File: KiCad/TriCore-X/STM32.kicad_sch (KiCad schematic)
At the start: 1 part, among them U7 STM32H723VGHx

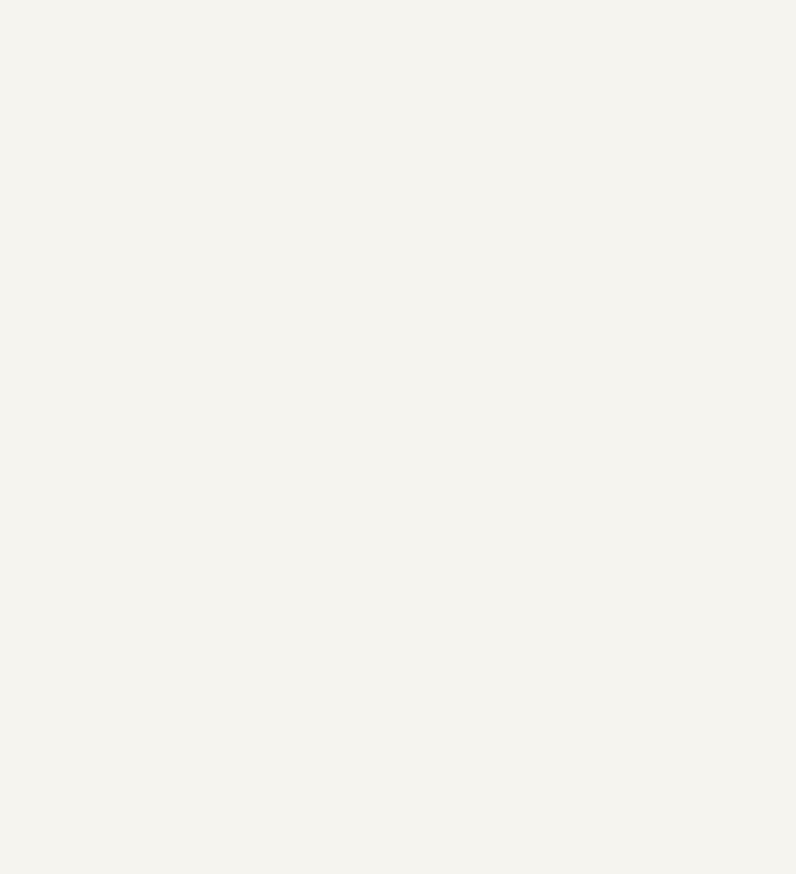
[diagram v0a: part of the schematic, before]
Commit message: feat: complete schematic for RK809-5 PMIC peripheral circuits
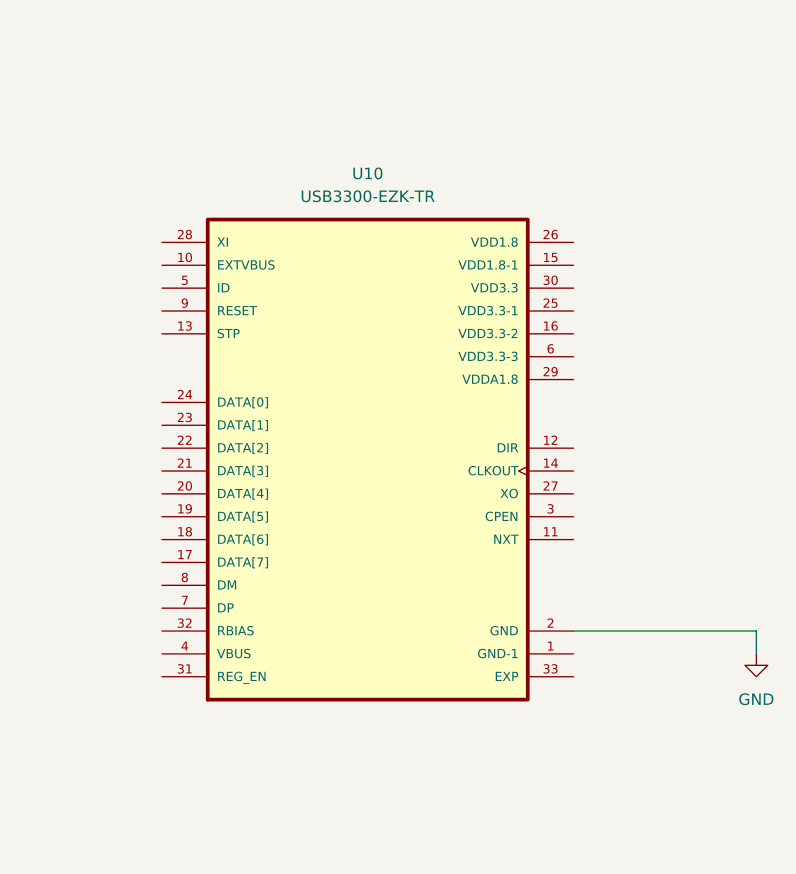
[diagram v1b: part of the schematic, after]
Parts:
- added U10: USB3300-EZK-TR, USB3300-EZK-TR:QFN50P500X500X100-33N, symbol USB3300-EZK-TR:USB3300-EZK-TR
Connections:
- net GND: now also U10.2 (GND)

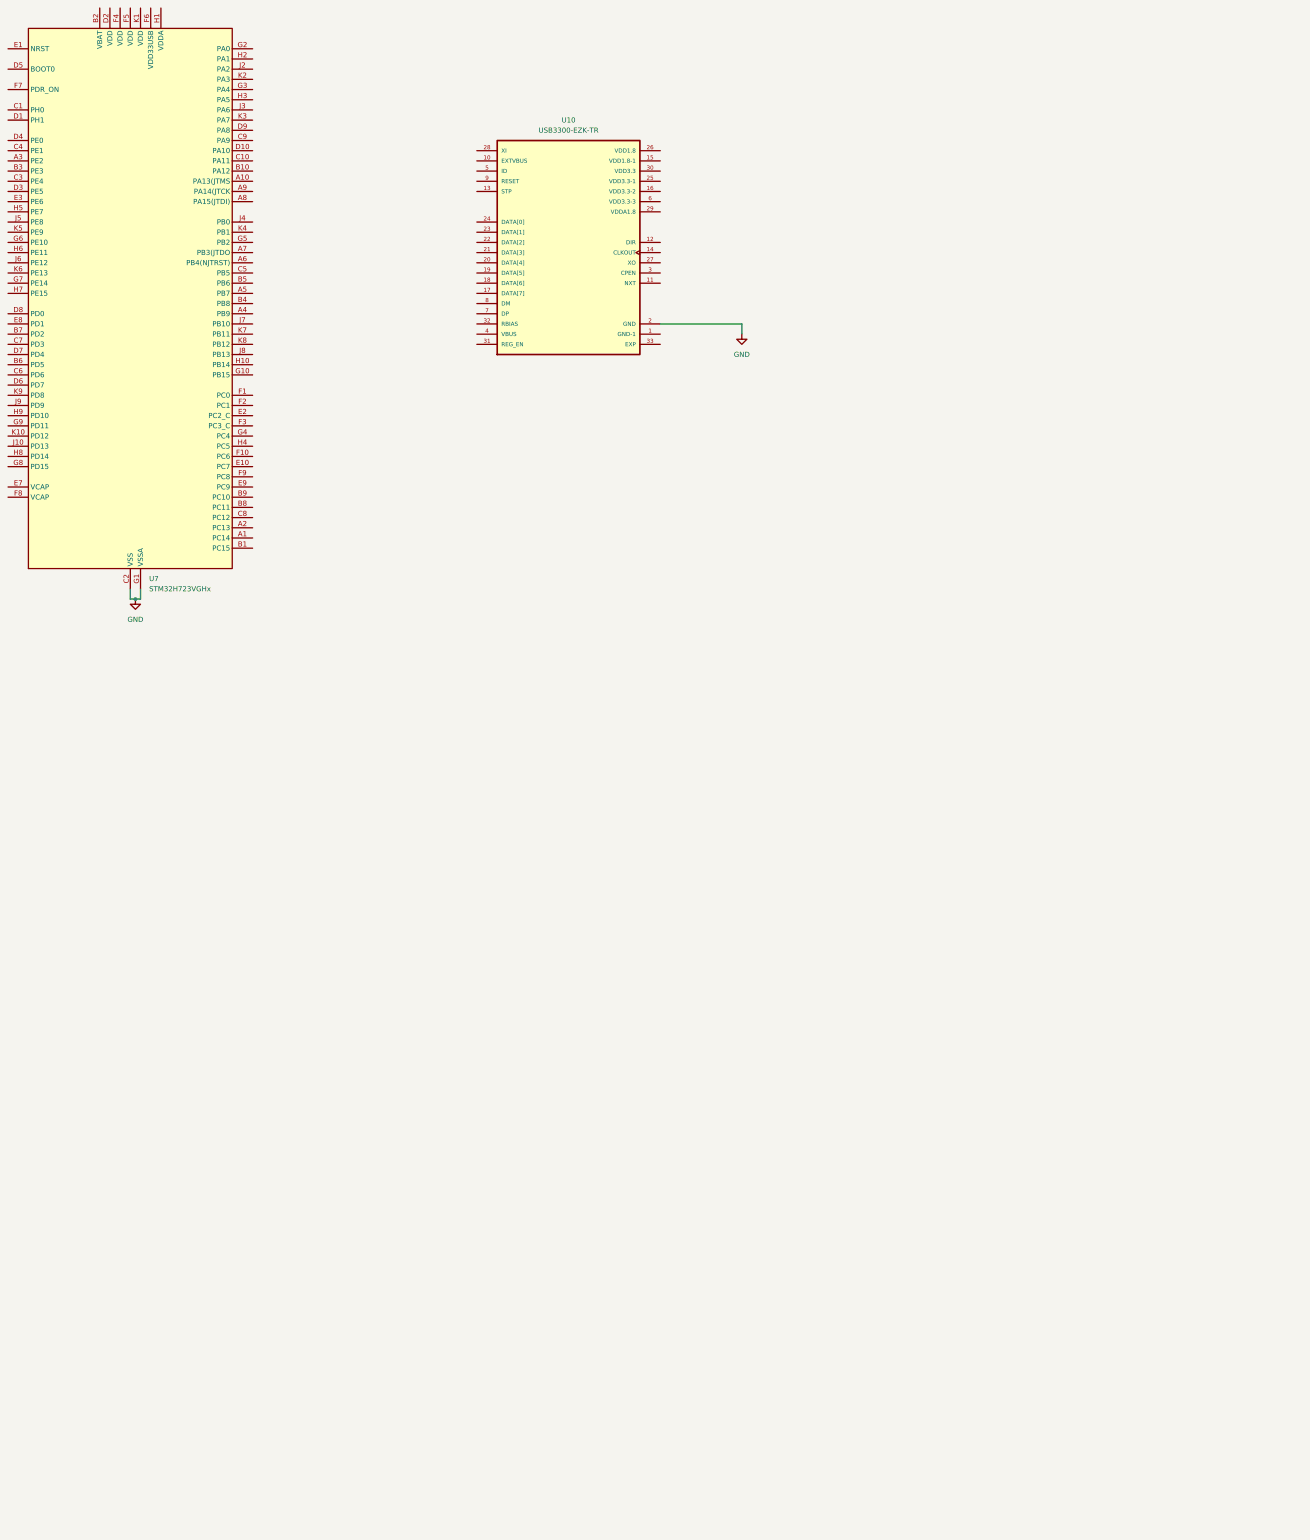
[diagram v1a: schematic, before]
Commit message: refactor: update schematic components and library references, including STM32H743 and new power symbols
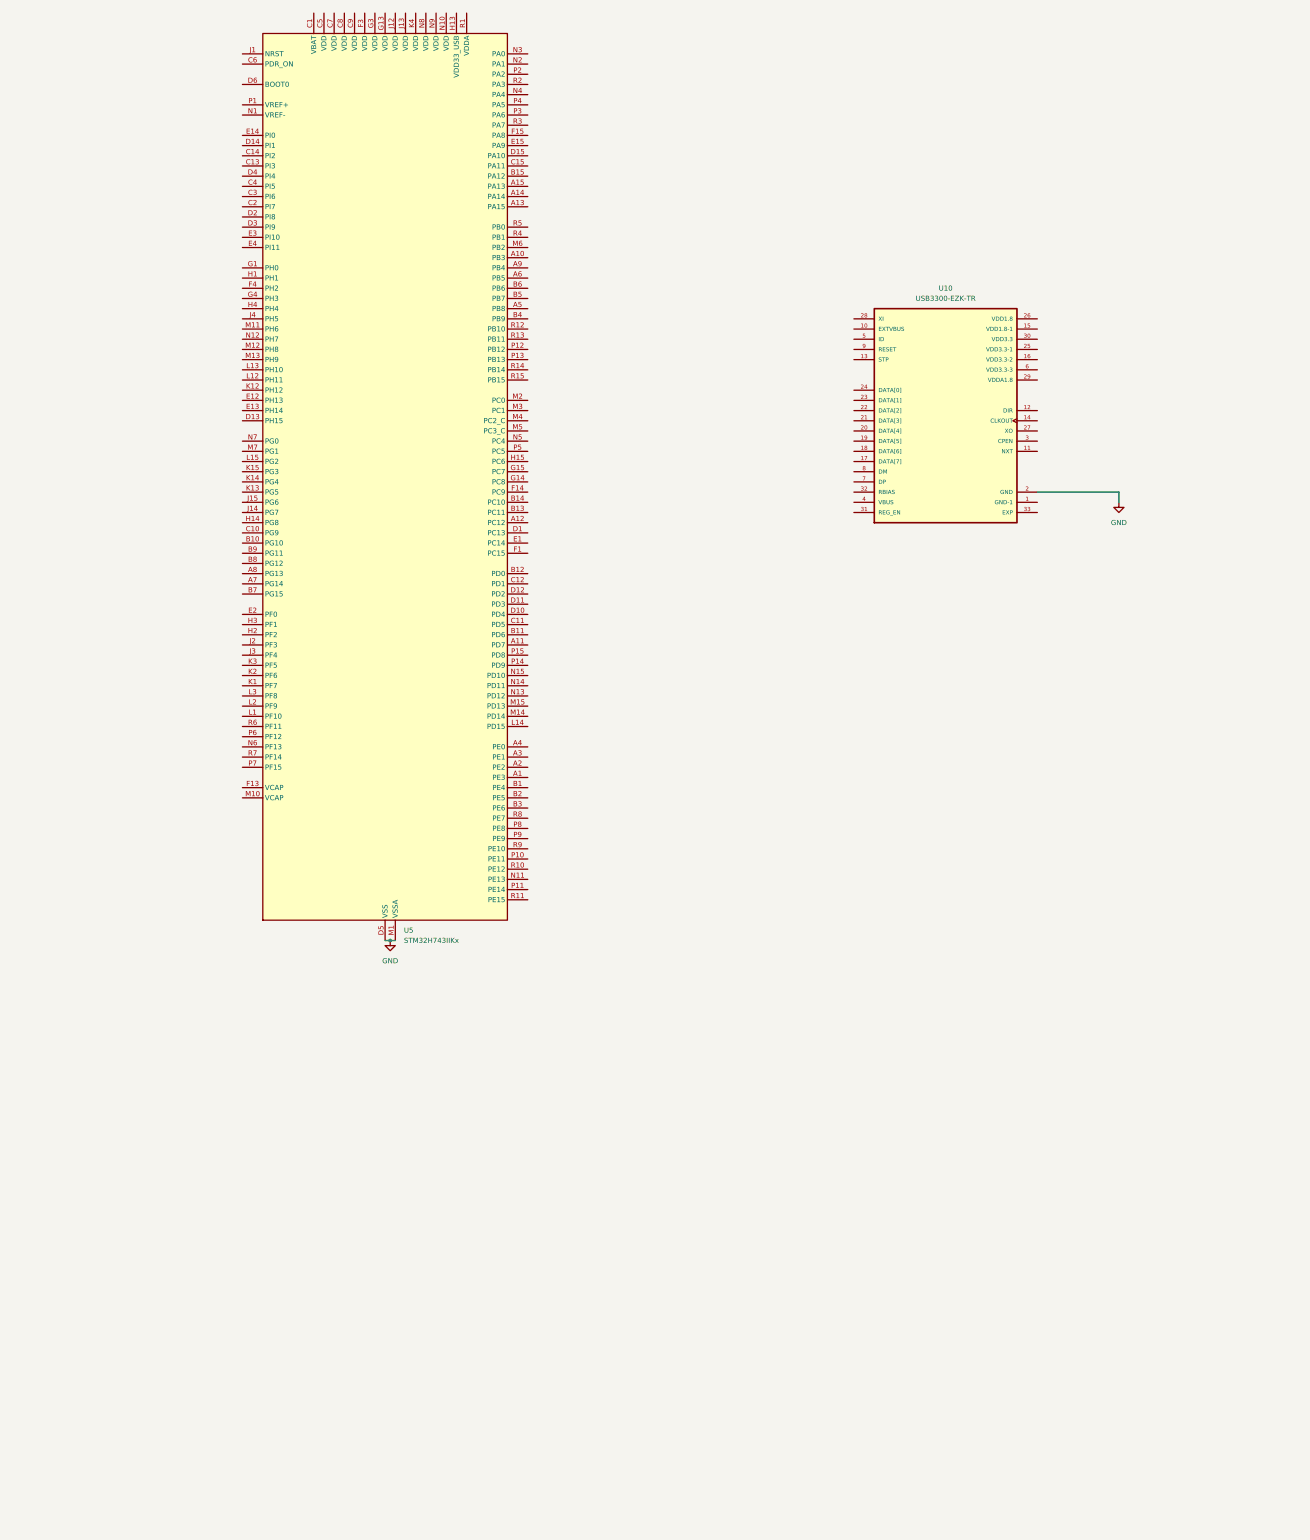
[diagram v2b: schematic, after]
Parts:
- removed U7: STM32H723VGHx, Package_BGA:TFBGA-100_8x8mm_Layout10x10_P0.8mm, symbol MCU_ST_STM32H7:STM32H723VGHx
- added U5: STM32H743IIKx, Package_BGA:UFBGA-201_10x10mm_Layout15x15_P0.65mm, symbol MCU_ST_STM32H7:STM32H743IIKx
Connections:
- net GND: now also U5.D5 (VSS), U5.D7 (VSS), U5.D8 (VSS), U5.D9 (VSS), U5.F10 (VSS), U5.F12 (VSS), U5.F2 (VSS), U5.F6 (VSS), U5.F7 (VSS), U5.F8 (VSS), U5.F9 (VSS), U5.G10 (VSS), U5.G12 (VSS), U5.G2 (VSS), U5.G6 (VSS), U5.G7 (VSS), U5.G8 (VSS), U5.G9 (VSS), U5.H10 (VSS), U5.H12 (VSS), U5.H6 (VSS), U5.H7 (VSS), U5.H8 (VSS), U5.H9 (VSS), U5.J10 (VSS), U5.J6 (VSS), U5.J7 (VSS), U5.J8 (VSS), U5.J9 (VSS), U5.K10 (VSS), U5.K6 (VSS), U5.K7 (VSS), U5.K8 (VSS), U5.K9 (VSS), U5.L4 (VSS), U5.M1 (VSSA), U5.M8 (VSS), U5.M9 (VSS)
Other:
- moved on the sheet: U10

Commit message: refactor: update schematic components, remove unused files, and add new LED and CH334P symbols
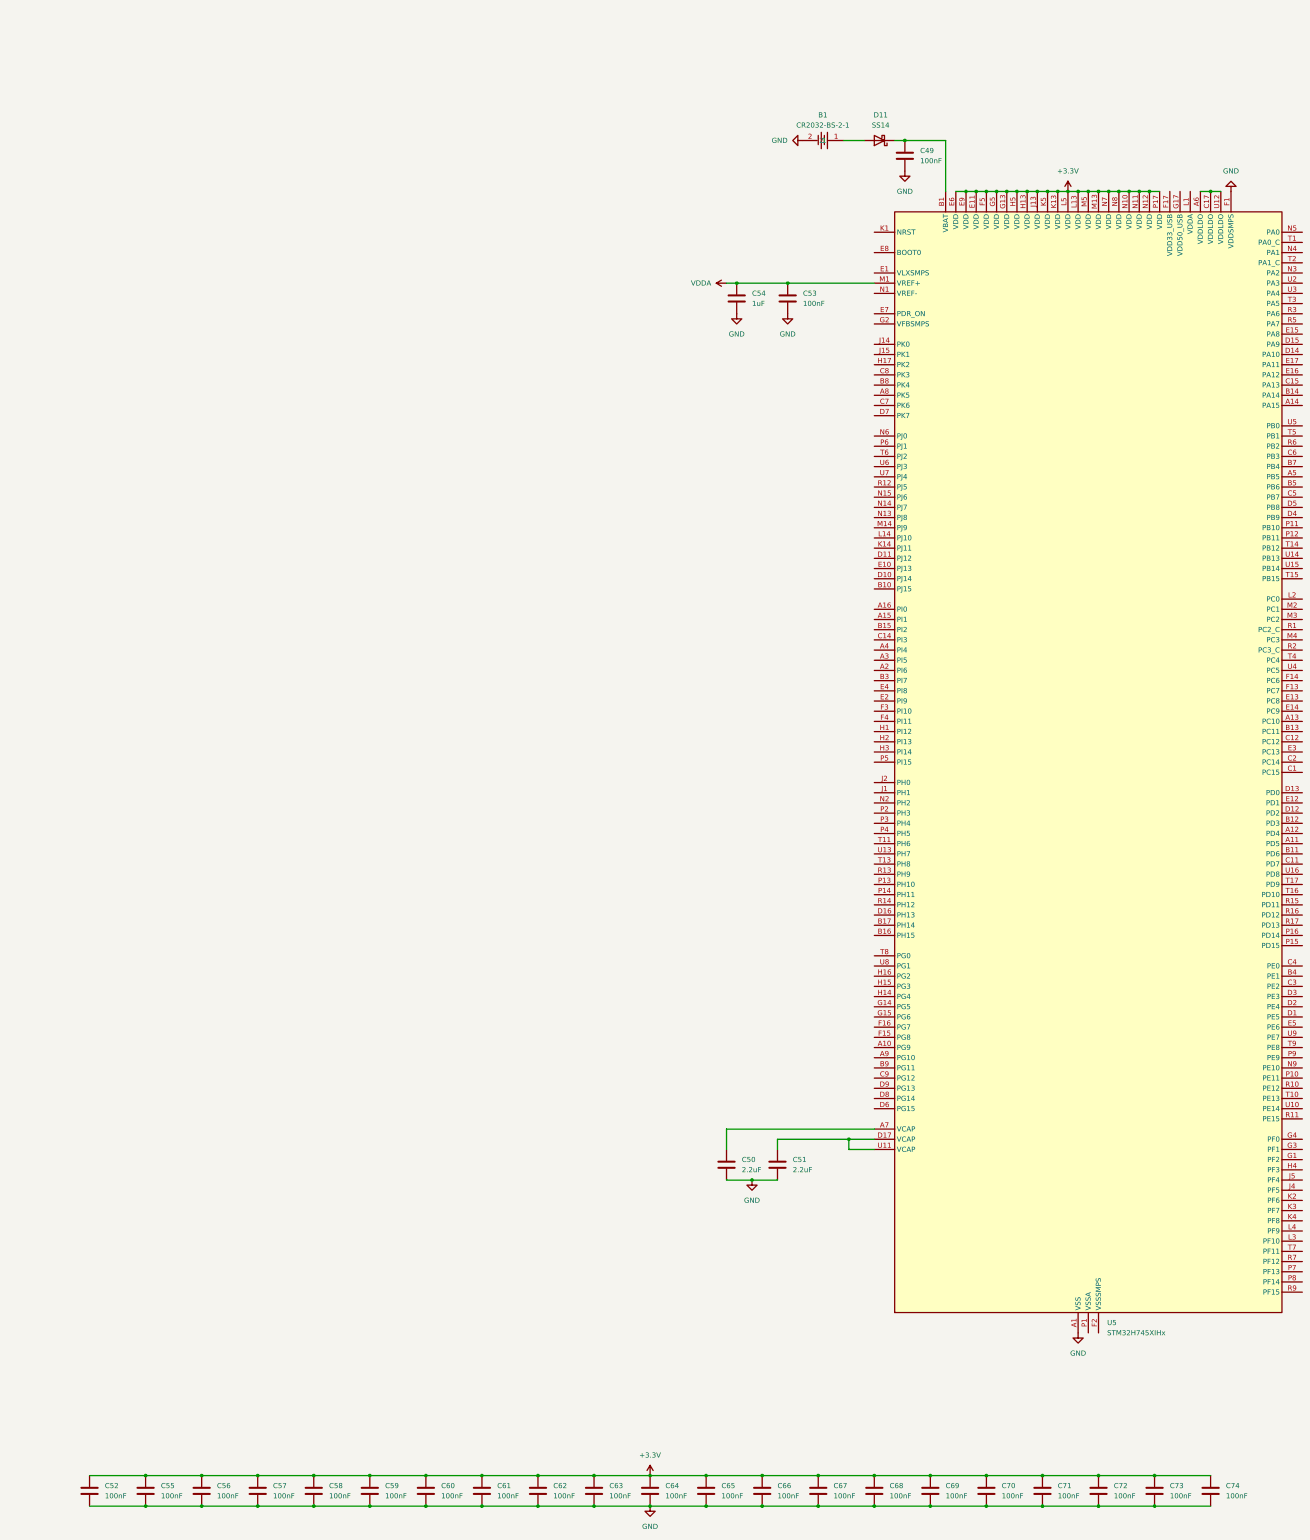
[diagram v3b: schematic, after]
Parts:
- removed U10: USB3300-EZK-TR, USB3300-EZK-TR:QFN50P500X500X100-33N, symbol USB3300-EZK-TR:USB3300-EZK-TR
- removed U5: STM32H743IIKx, Package_BGA:UFBGA-201_10x10mm_Layout15x15_P0.65mm, symbol MCU_ST_STM32H7:STM32H743IIKx
- added B1: CR2032-BS-2-1, Battery Holder BS-2-1:BAT-TH_BS-2-1, symbol Battery Holder BS-2-1:CR2032-BS-2-1
- added C49, C52, C53, C55, C56, C57, C58, C59, C60, C61, C62, C63, C64, C65, C66, C67, C68, C69, C70, C71, C72, C73, C74: 100nF, Capacitor_SMD:C_0402_1005Metric, symbol Device:C
- added C50, C51: 2.2uF, Capacitor_SMD:C_0402_1005Metric, symbol Device:C
- added C54: 1uF, Capacitor_SMD:C_0402_1005Metric, symbol Device:C
- added D11: SS14, Diode_SMD:D_SMA, symbol Diode:SS14
- added U5: STM32H745XIHx, Package_BGA:TFBGA-265_14x14mm_Layout17x17_P0.8mm, symbol MCU_ST_STM32H7:STM32H745XIHx
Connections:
- net GND: now also B1.2, C49.2, C50.1, C51.2, C52.2, C53.2, C54.2, C55.2, C56.2, C57.2, C58.2, C59.2, C60.2, C61.2, C62.2, C63.2, C64.2, C65.2, C66.2, C67.2, C68.2, C69.2, C70.2, C71.2, C72.2, C73.2, C74.2, U5.A1 (VSS), U5.A17 (VSS), U5.B2 (VSS), U5.B6 (VSS), U5.C10 (VSS), U5.C13 (VSS), U5.C16 (VSS), U5.F1 (VDDSMPS), U5.G10 (VSS), U5.G11 (VSS), U5.G16 (VSS), U5.G7 (VSS), U5.G8 (VSS), U5.G9 (VSS), U5.H10 (VSS), U5.H11 (VSS), U5.H7 (VSS), U5.H8 (VSS), U5.H9 (VSS), U5.J10 (VSS), U5.J11 (VSS), U5.J16 (VSS), U5.J17 (VSS), U5.J3 (VSS), U5.J7 (VSS), U5.J8 (VSS), U5.J9 (VSS), U5.K10 (VSS), U5.K11 (VSS), U5.K15 (VSS), U5.K7 (VSS), U5.K8 (VSS), U5.K9 (VSS), U5.L10 (VSS), U5.L11 (VSS), U5.L15 (VSS), U5.L7 (VSS), U5.L8 (VSS), U5.L9 (VSS), U5.M15 (VSS), U5.N16 (VSS), U5.R4 (VSS), U5.R8 (VSS), U5.T12 (VSS), U5.U1 (VSS), U5.U17 (VSS)
- new net: C51.1, U5.D17 (VCAP), U5.U11 (VCAP)
- new net: C49.1, D11.1 (K), U5.B1 (VBAT)
- new net: B1.1, D11.2 (A)
- new net: U5.A6 (VDDLDO), U5.C17 (VDDLDO), U5.U12 (VDDLDO)
- new net: C50.2, U5.A7 (VCAP)
- new net +3.3V: C52.1, C55.1, C56.1, C57.1, C58.1, C59.1, C60.1, C61.1, C62.1, C63.1, C64.1, C65.1, C66.1, C67.1, C68.1, C69.1, C70.1, C71.1, C72.1, C73.1, C74.1, U5.E11 (VDD), U5.E6 (VDD), U5.E9 (VDD), U5.F5 (VDD), U5.G13 (VDD), U5.G5 (VDD), U5.H13 (VDD), U5.H5 (VDD), U5.J13 (VDD), U5.K13 (VDD), U5.K5 (VDD), U5.L13 (VDD), U5.L5 (VDD), U5.M13 (VDD), U5.M5 (VDD), U5.N10 (VDD), U5.N11 (VDD), U5.N12 (VDD), U5.N7 (VDD), U5.N8 (VDD), U5.P17 (VDD)
- new net VDDA: C53.1, C54.1, U5.M1 (VREF+)
